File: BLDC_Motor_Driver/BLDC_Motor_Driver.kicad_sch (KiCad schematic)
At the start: 32 parts, among them J1 Conn_01x03_Socket, J2 Conn_01x05_Socket, Q1 CSD18540Q5B, Q10 CSD18540Q5B, Q2 CSD18540Q5B, Q3 CSD18540Q5B, Q4 CSD18540Q5B, Q5 CSD18540Q5B, Q6 CSD18540Q5B, Q7 CSD18540Q5B, Q8 CSD18540Q5B, Q9 CSD18540Q5B, U1 TMC9660ATB+T, U101 TMC9660

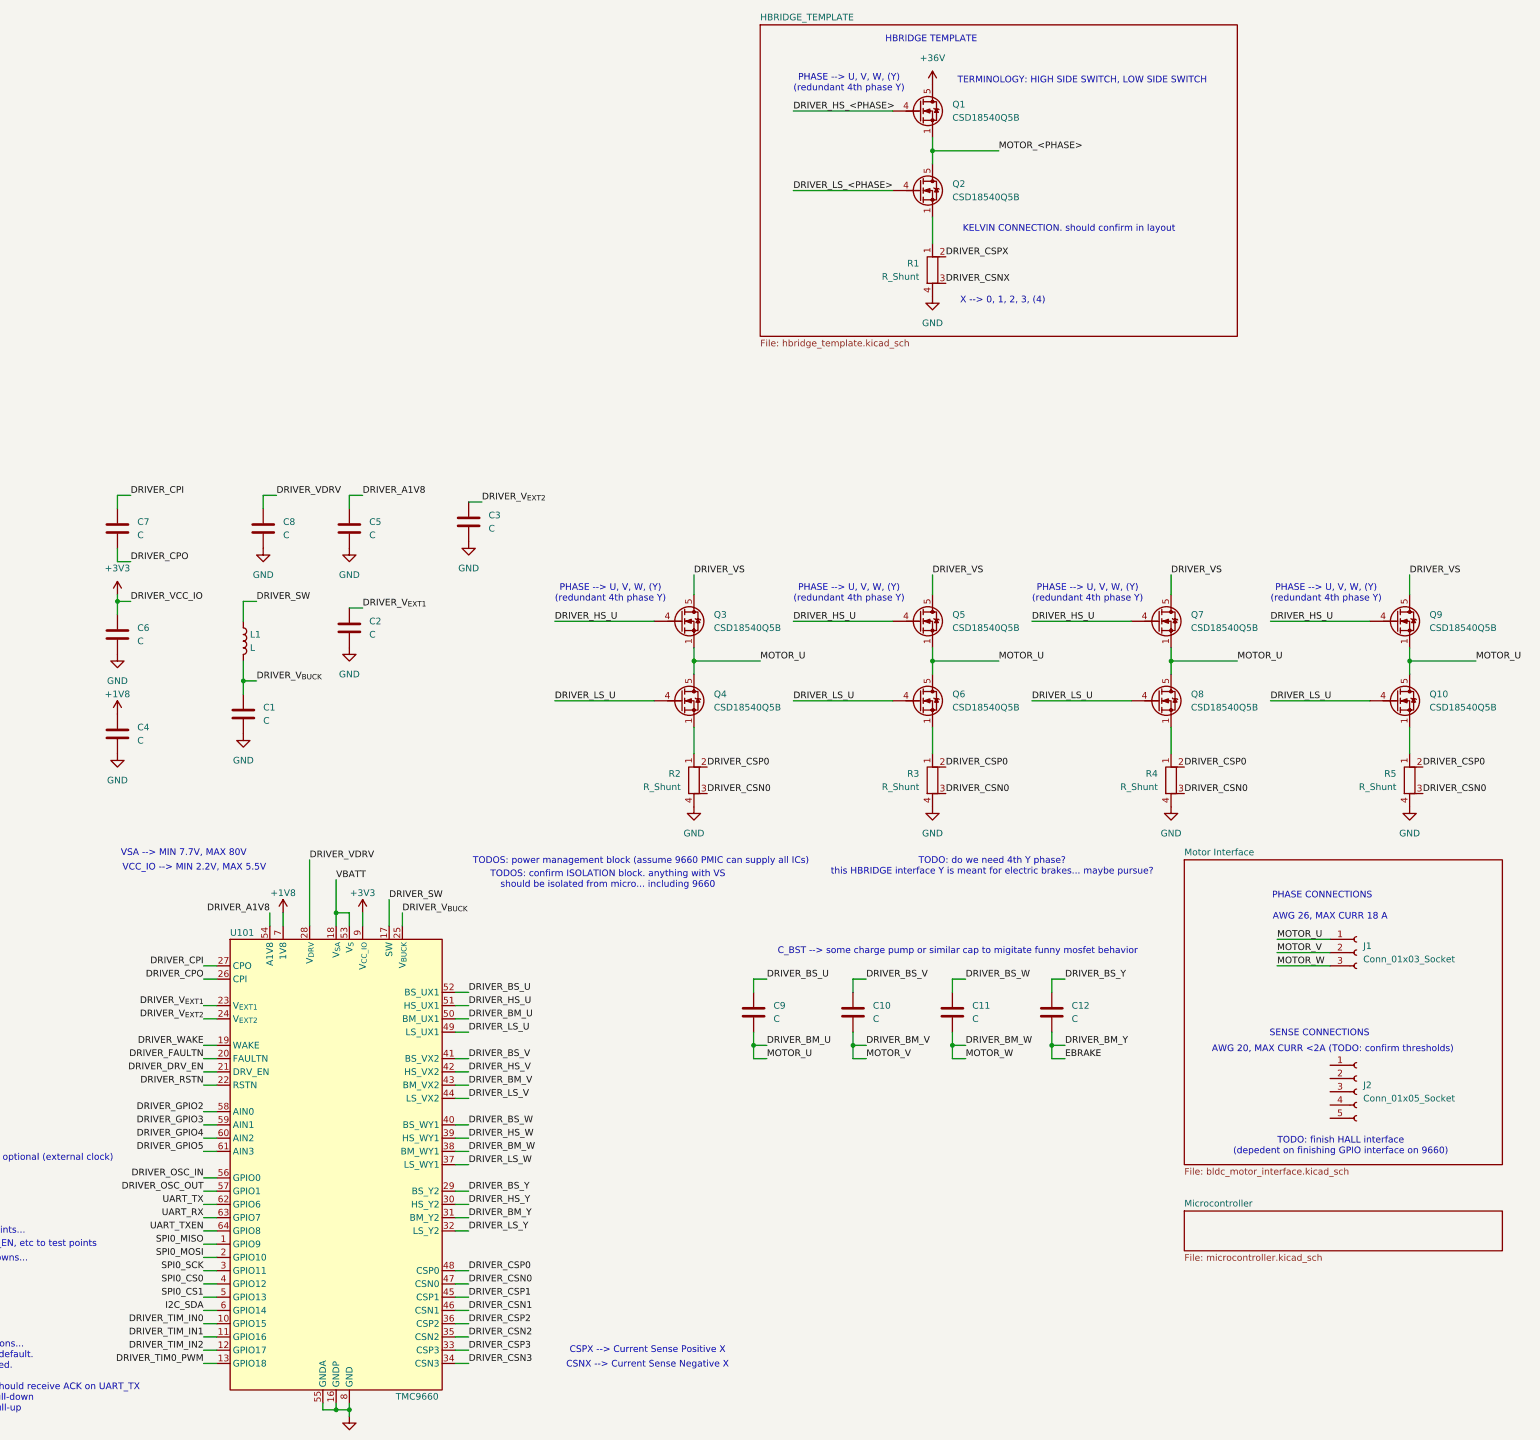
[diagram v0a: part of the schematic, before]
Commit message: reorganized schematic, added some passive footprints & values
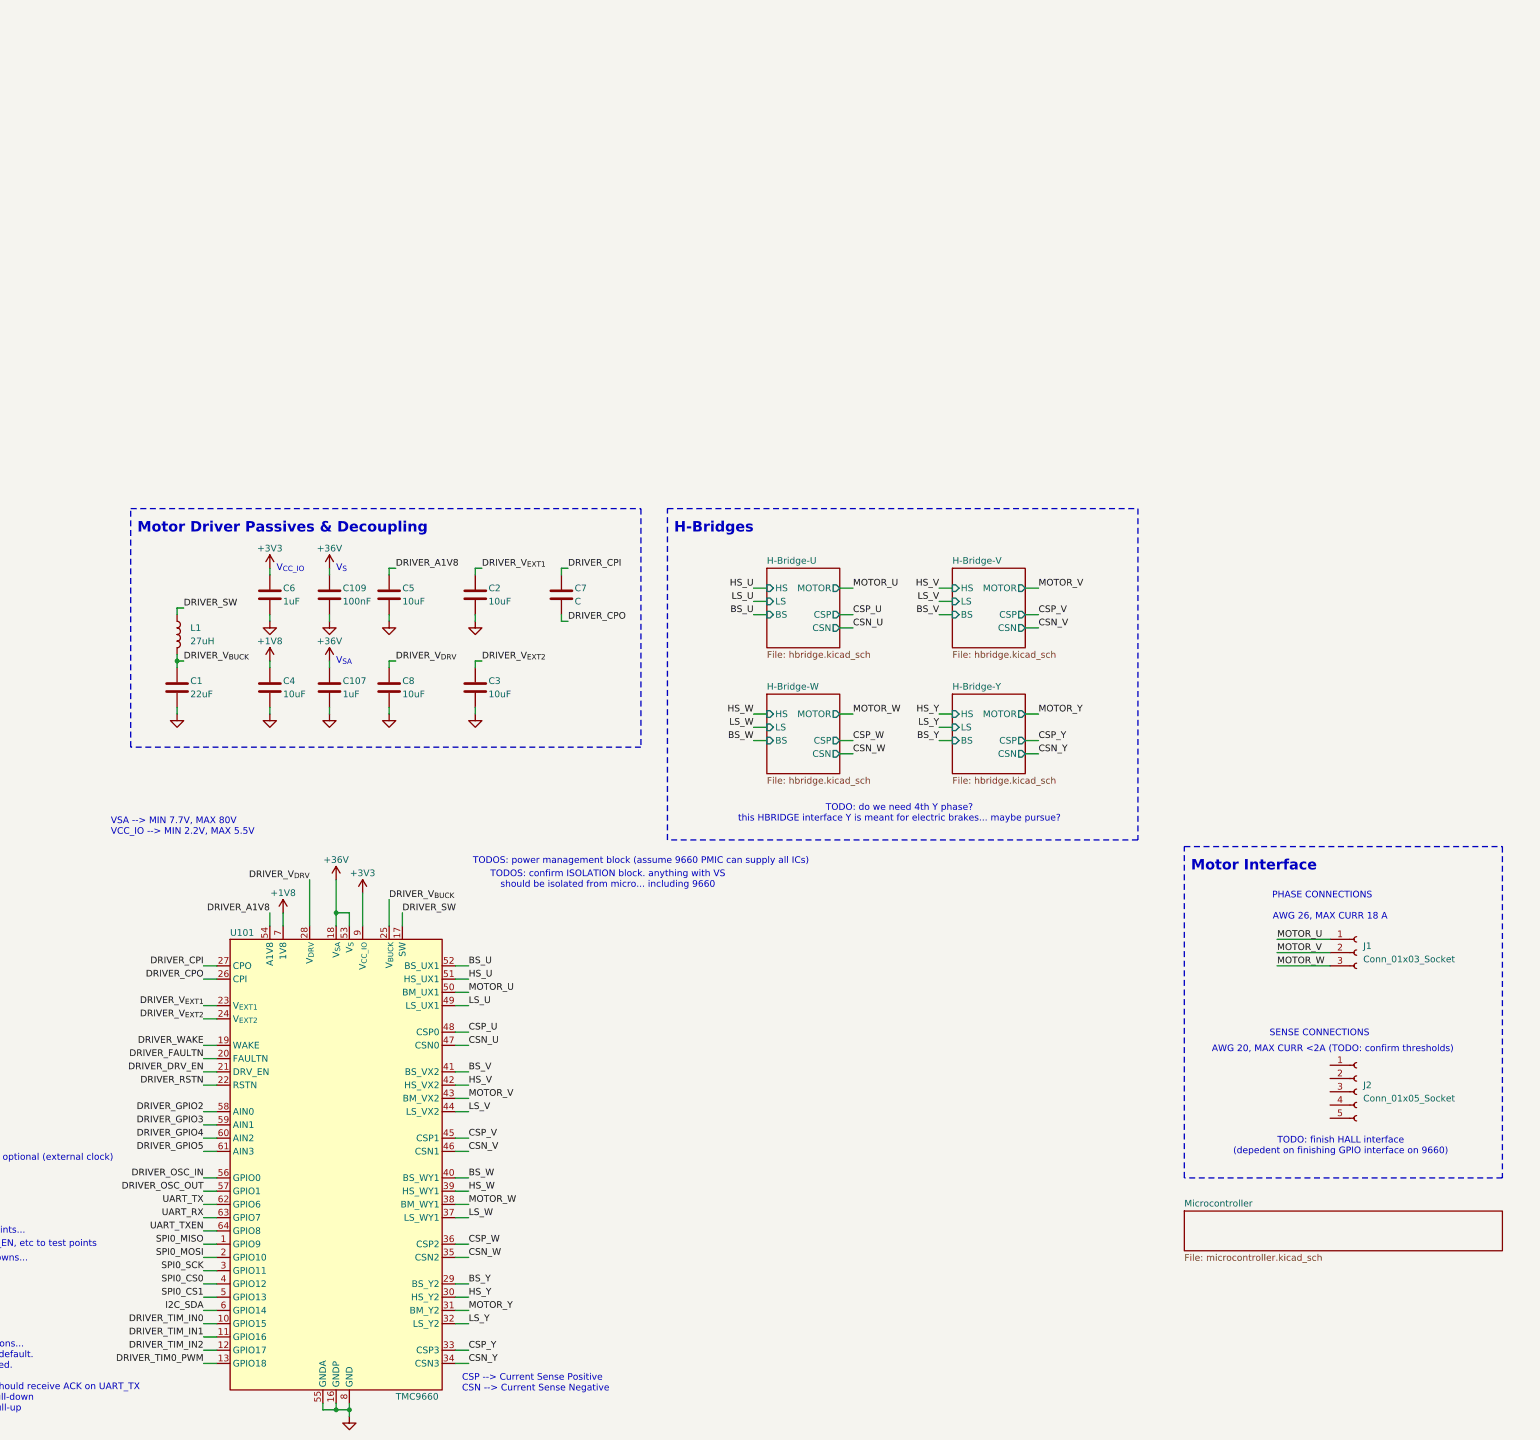
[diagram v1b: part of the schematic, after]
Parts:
- removed C10, C11, C12, C9: C, symbol Device:C
- removed Q1, Q10, Q2, Q3, Q4, Q5, Q6, Q7, Q8, Q9: CSD18540Q5B, Package_TO_SOT_SMD:TDSON-8-1, symbol Transistor_FET:CSD18540Q5B
- removed R1, R2, R3, R4, R5: R_Shunt, symbol Device:R_Shunt
- added C107: 1uF, Capacitor_SMD:C_1206_3216Metric, symbol Device:C
- added C109: 100nF, Capacitor_SMD:C_0805_2012Metric, symbol Device:C
- C1: value C -> 22uF; footprint (none) -> Capacitor_SMD:C_0805_2012Metric
- C2, C3: value C -> 10uF; footprint (none) -> Capacitor_SMD:C_0603_1608Metric
- C4, C5: value C -> 10uF; footprint (none) -> Capacitor_SMD:C_0805_2012Metric
- C6: value C -> 1uF; footprint (none) -> Capacitor_SMD:C_0603_1608Metric
- C8: value C -> 10uF
- L1: value L -> 27uH; footprint (none) -> Inductor_SMD:L_APV_ANR6045
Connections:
- net VBATT is gone; now on net +36V: U101.18 (V_{SA}), U101.53 (V_{S})
- net +36V: now also C107.1, C109.1
- net +3V3: no longer U1.9 (VCC_IO)
- net DRIVER_BM_U: no longer J1.1 (Pin_1), U101.50 (BM_UX1)
- net DRIVER_BM_V: no longer J1.2 (Pin_2), U101.43 (BM_VX2)
- net DRIVER_BM_W: no longer J1.3 (Pin_3), U101.38 (BM_WY1)
- net DRIVER_BM_Y: no longer U101.31 (BM_Y2)
- net DRIVER_BS_U: no longer U101.52 (BS_UX1)
- net DRIVER_BS_V: no longer U101.41 (BS_VX2)
- net DRIVER_BS_W: no longer U101.40 (BS_WY1)
- net DRIVER_BS_Y: no longer U101.29 (BS_Y2)
- net DRIVER_CSN0: no longer U101.47 (CSN0)
- net DRIVER_CSN1: no longer U101.46 (CSN1)
- net DRIVER_CSN2: no longer U101.35 (CSN2)
- net DRIVER_CSN3: no longer U101.34 (CSN3)
- net DRIVER_CSP0: no longer U101.48 (CSP0)
- net DRIVER_CSP1: no longer U101.45 (CSP1)
- net DRIVER_CSP2: no longer U101.36 (CSP2)
- net DRIVER_CSP3: no longer U101.33 (CSP3)
- net DRIVER_HS_U: no longer U101.51 (HS_UX1)
- net DRIVER_HS_V: no longer U101.42 (HS_VX2)
- net DRIVER_HS_W: no longer U101.39 (HS_WY1)
- net DRIVER_HS_Y: no longer U101.30 (HS_Y2)
- net DRIVER_LS_U: no longer U101.49 (LS_UX1)
- net DRIVER_LS_V: no longer U101.44 (LS_VX2)
- net DRIVER_LS_W: no longer U101.37 (LS_WY1)
- net DRIVER_LS_Y: no longer U101.32 (LS_Y2)
- net DRIVER_VDRV: no longer C8.1, U101.28 (V_{DRV})
- net GND: now also C107.2, C109.2
- new net BS_U: U101.52 (BS_UX1)
- new net BS_V: U101.41 (BS_VX2)
- new net BS_W: U101.40 (BS_WY1)
- new net BS_Y: U101.29 (BS_Y2)
- new net CSN_U: U101.47 (CSN0)
- new net CSN_V: U101.46 (CSN1)
- new net CSN_W: U101.35 (CSN2)
- new net CSN_Y: U101.34 (CSN3)
- new net CSP_U: U101.48 (CSP0)
- new net CSP_V: U101.45 (CSP1)
- new net CSP_W: U101.36 (CSP2)
- new net CSP_Y: U101.33 (CSP3)
- new net DRIVER_VCC_IO: U1.9 (VCC_IO)
- new net DRIVER_V_{DRV}: C8.1, U101.28 (V_{DRV})
- new net HS_U: U101.51 (HS_UX1)
- new net HS_V: U101.42 (HS_VX2)
- new net HS_W: U101.39 (HS_WY1)
- new net HS_Y: U101.30 (HS_Y2)
- new net LS_U: U101.49 (LS_UX1)
- new net LS_V: U101.44 (LS_VX2)
- new net LS_W: U101.37 (LS_WY1)
- new net LS_Y: U101.32 (LS_Y2)
- new net MOTOR_U: J1.1 (Pin_1), U101.50 (BM_UX1)
- new net MOTOR_V: J1.2 (Pin_2), U101.43 (BM_VX2)
- new net MOTOR_W: J1.3 (Pin_3), U101.38 (BM_WY1)
- new net MOTOR_Y: U101.31 (BM_Y2)
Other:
- sheet HBRIDGE_TEMPLATE renamed H-Bridge-U
- removed sheet Motor Interface
- added sheet H-Bridge-V (hbridge.kicad_sch)
- added sheet H-Bridge-W (hbridge.kicad_sch)
- added sheet H-Bridge-Y (hbridge.kicad_sch)
- sheet H-Bridge-U: file hbridge_template.kicad_sch -> hbridge.kicad_sch
- sheet H-Bridge-U ports: added BS, CSN, CSP, HS, LS, MOTOR; removed none
- note added: "CSP --> Current Sense Positive CSN --> Current Sense Negative"
- note added: "H-Bridges"
- note added: "Motor Driver Passives & Decoupling"
- note added: "Motor Interface"
- note added: "VSA --> MIN 7.7V, MAX 80V VCC_IO --> MIN 2.2V, MAX 5.5V"
- note added: "V_{CC_IO}"
- note added: "V_{SA}"
- note added: "V_{S}"
- note removed: "CSNX --> Current Sense Negative X"
- note removed: "CSPX --> Current Sense Positive X"
- note removed: "C_BST --> some charge pump or similar cap to migitate funny mosfet behavior"
- note removed: "HBRIDGE TEMPLATE"
- note removed: "KELVIN CONNECTION. should confirm in layout"
- note removed: "PHASE --> U, V, W, (Y) (redundant 4th phase Y)"
- note removed: "TERMINOLOGY: HIGH SIDE SWITCH, LOW SIDE SWITCH"
- note removed: "VCC_IO --> MIN 2.2V, MAX 5.5V"
- note removed: "VSA --> MIN 7.7V, MAX 80V"
- note removed: "X --> 0, 1, 2, 3, (4)"
- moved on the sheet: C1, C2, C3, C4, C5, C6, C7, C8, L1

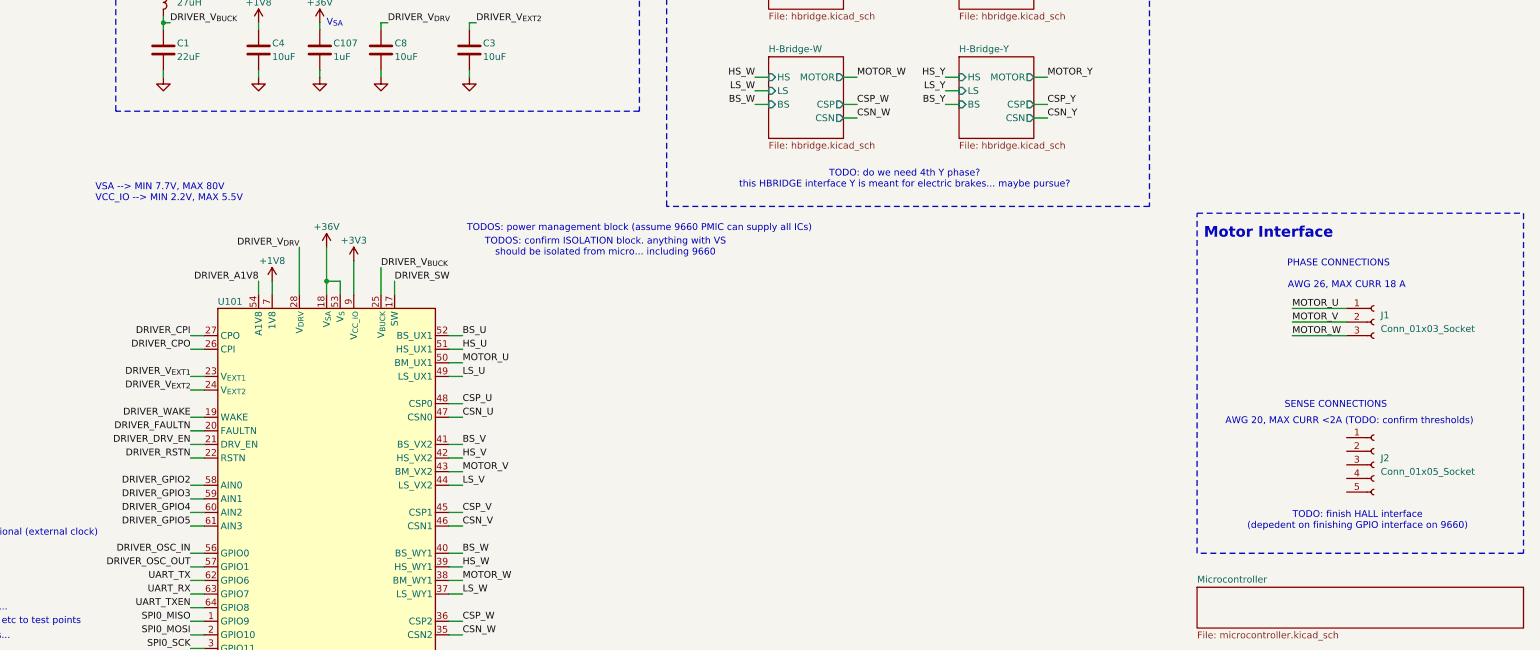
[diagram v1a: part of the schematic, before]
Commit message: started hall effect and power circuitry
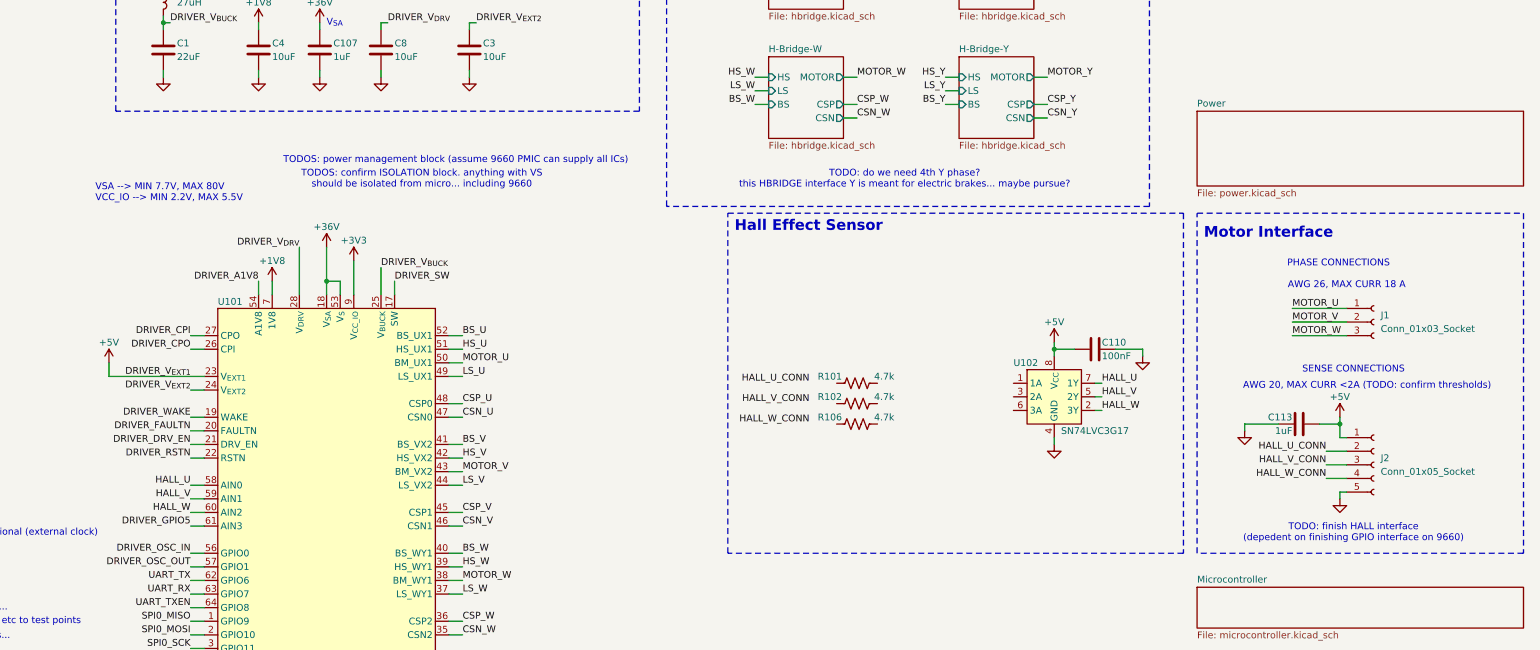
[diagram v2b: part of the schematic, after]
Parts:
- added C110: 100nF, Capacitor_SMD:C_0603_1608Metric, symbol Device:C
- added C113: 1uF, Capacitor_SMD:C_0603_1608Metric, symbol Device:C
- added R101, R102, R106: 4.7k, Resistor_SMD:R_0603_1608Metric, symbol Device:R_US
- added U102: SN74LVC3G17, Package_SO:VSSOP-8_2.3x2mm_P0.5mm, symbol Buffer_Texas:SN74LVC3G17
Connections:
- net DRIVER_V_{EXT1} is gone; now on net +5V: C2.1, U101.23 (V_{EXT1})
- net DRIVER_GPIO2: no longer U101.58 (AIN0)
- net DRIVER_GPIO3: no longer U101.59 (AIN1)
- net DRIVER_GPIO4: no longer U101.60 (AIN2)
- net GND: now also J2.5 (Pin_5), C110.2, C113.2, U102.4 (GND)
- net +5V: now reaches J2.1 (Pin_1)
- net +5V: now also C110.1, C113.1, U102.8 (V_{CC})
- net HALL_U_CONN: now reaches J2.2 (Pin_2)
- net HALL_V_CONN: now reaches J2.3 (Pin_3)
- net HALL_W_CONN: now reaches J2.4 (Pin_4)
- new net HALL_U: U101.58 (AIN0), U102.7 (1Y)
- new net HALL_V: U101.59 (AIN1), U102.5 (2Y)
- new net HALL_W: U101.60 (AIN2), U102.2 (3Y)
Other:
- added sheet Power (power.kicad_sch)
- note added: "Hall Effect Sensor"
